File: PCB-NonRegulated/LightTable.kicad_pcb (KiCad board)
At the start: 2 copper layers, 19 parts, among them CON1 BARREL_JACK, P1 CONN_2_V, P2 CONN_01X01, P3 CONN_01X01, P4 CONN_01X01, P5 CONN_01X01, P6 CONN_01X01, P7 CONN_01X01, P8 CONN_4_V, U1 MosfetIRF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

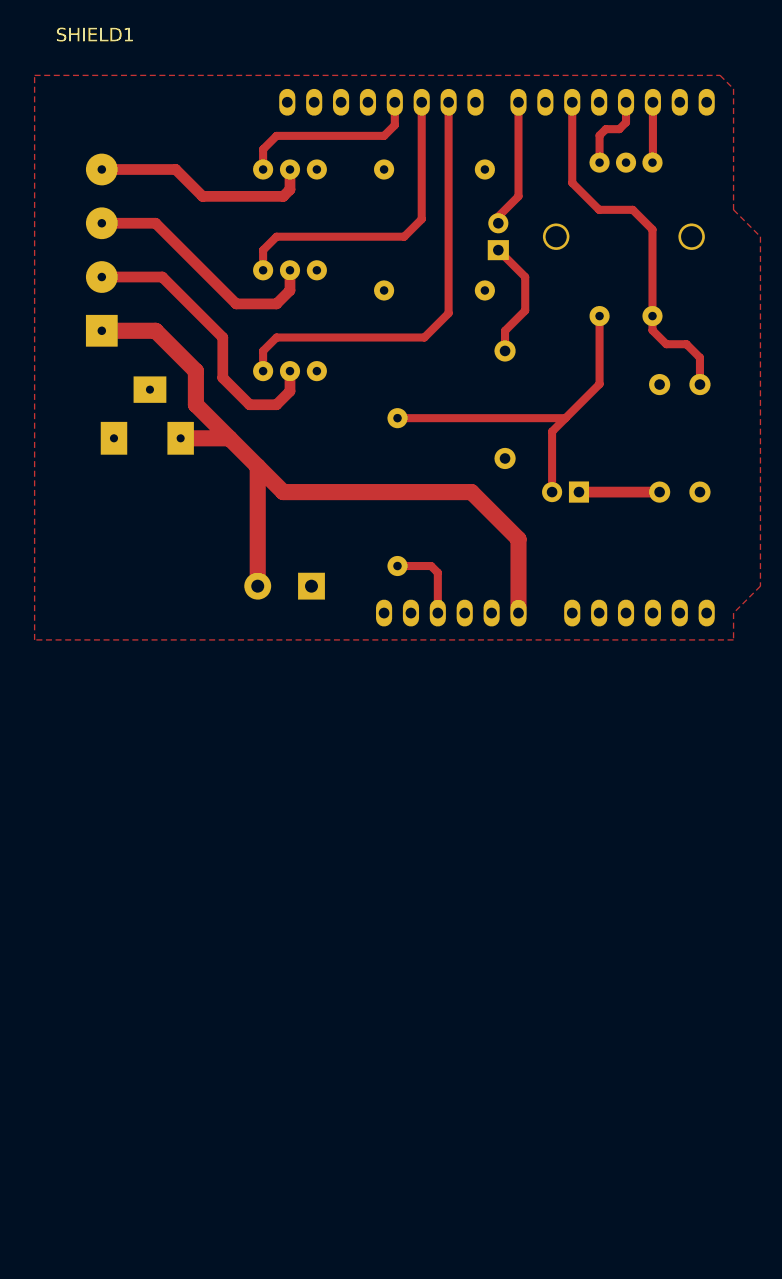
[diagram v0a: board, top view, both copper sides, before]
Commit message: Fixed wrong placement of shield and added gerbers
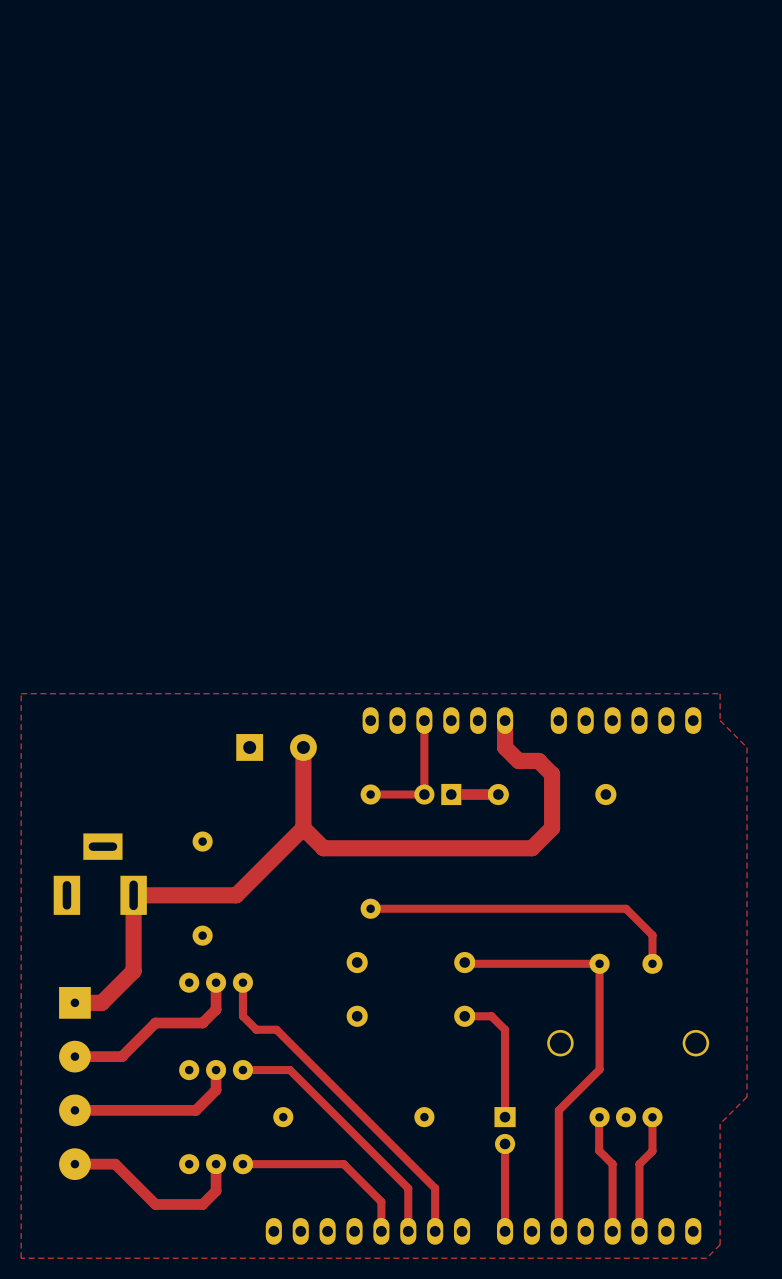
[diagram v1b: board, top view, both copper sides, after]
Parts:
- SHIELD1: moved to B.Cu
- moved P2 90.0 mm to (95.9, 149.2)
- moved P3 89.7 mm to (109.2, 149.2)
- moved D2 81.9 mm to (116.8, 149.2), turned to 270 degrees
- moved P8 78.8 mm to (76.2, 146.1)
- moved U1 76.9 mm to (92.1, 136.5), turned to 180 degrees
- moved EN1 76.2 mm to (128.3, 142.2), turned to 90 degrees
- moved U2 75.6 mm to (92.1, 144.8), turned to 180 degrees
- moved U3 75.0 mm to (92.1, 153.7), turned to 180 degrees
- moved P7 66.5 mm to (88.3, 132.1)
- moved R3 58.5 mm to (108.0, 139.7), turned to 180 degrees
- moved R1 56.6 mm to (108.0, 134.6), turned to 180 degrees
- moved P4 54.8 mm to (88.3, 123.2)
- moved P5 46.4 mm to (104.1, 129.5)
- moved CON1 43.4 mm to (67.9, 128.3)
- moved R2 35.2 mm to (121.3, 118.7), turned to 0 degrees
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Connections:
- SHIELD1 pad 11: PWM_R -> PWM_B
- SHIELD1 pad 9: PWM_B -> PWM_R
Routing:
- net PWM_B: track 40.8 -> 17.3 mm
- net PWM_R: track 17.5 -> 32.1 mm
- net B: track 27.4 -> 18.0 mm
- net G: track 23.4 -> 16.0 mm
- net +12V: track 72.3 -> 78.4 mm
- net Net-(EN1-Pad3): track 5.72 -> 11.3 mm
- net PBtn: track 34.6 -> 39.7 mm
- net PWM_G: track 29.1 -> 24.3 mm
- net Net-(D2-Pad2): track 12.2 -> 8.26 mm
- net Net-(EN1-Pad1): track 7.48 -> 11.3 mm
- net R: track 21.0 -> 17.7 mm
- net Net-(D1-Pad1): track 7.62 -> 4.44 mm
- net Net-(D2-Pad1): track 11.4 -> 12.6 mm
